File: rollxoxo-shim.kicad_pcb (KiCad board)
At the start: 4 copper layers, 70 parts, among them J1 USB_C_Receptacle_USB2.0_14P, J2 Conn_01x02, J3 Conn_01x10, J4 Conn_01x01, J5 Conn_01x10, J6 Conn_01x03, J7 Conn_01x01, SW1 SW_Push, SW2 SW_Push, U1 SN74LV1T125DBV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

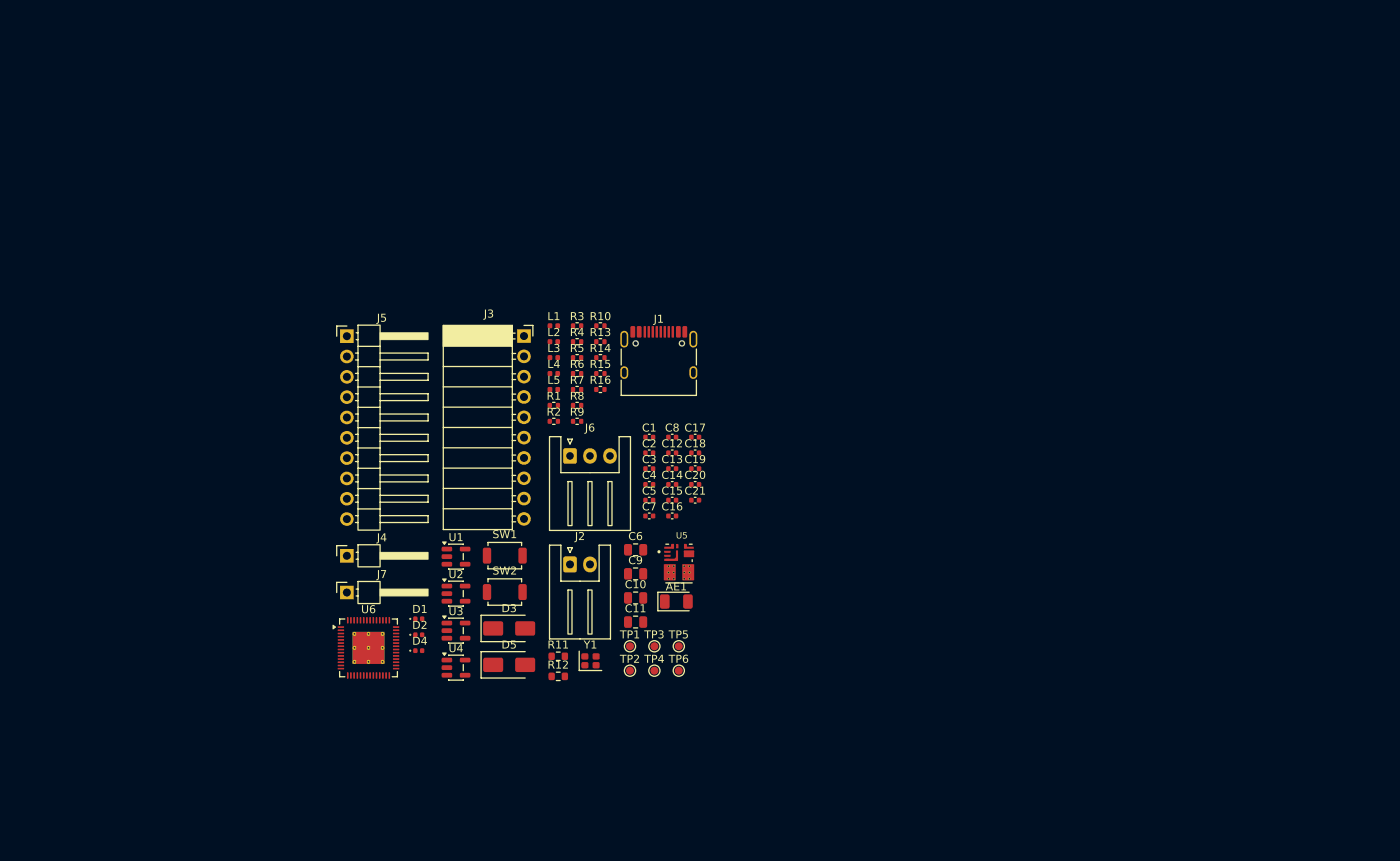
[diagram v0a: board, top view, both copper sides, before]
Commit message: pcb: initial rough placement
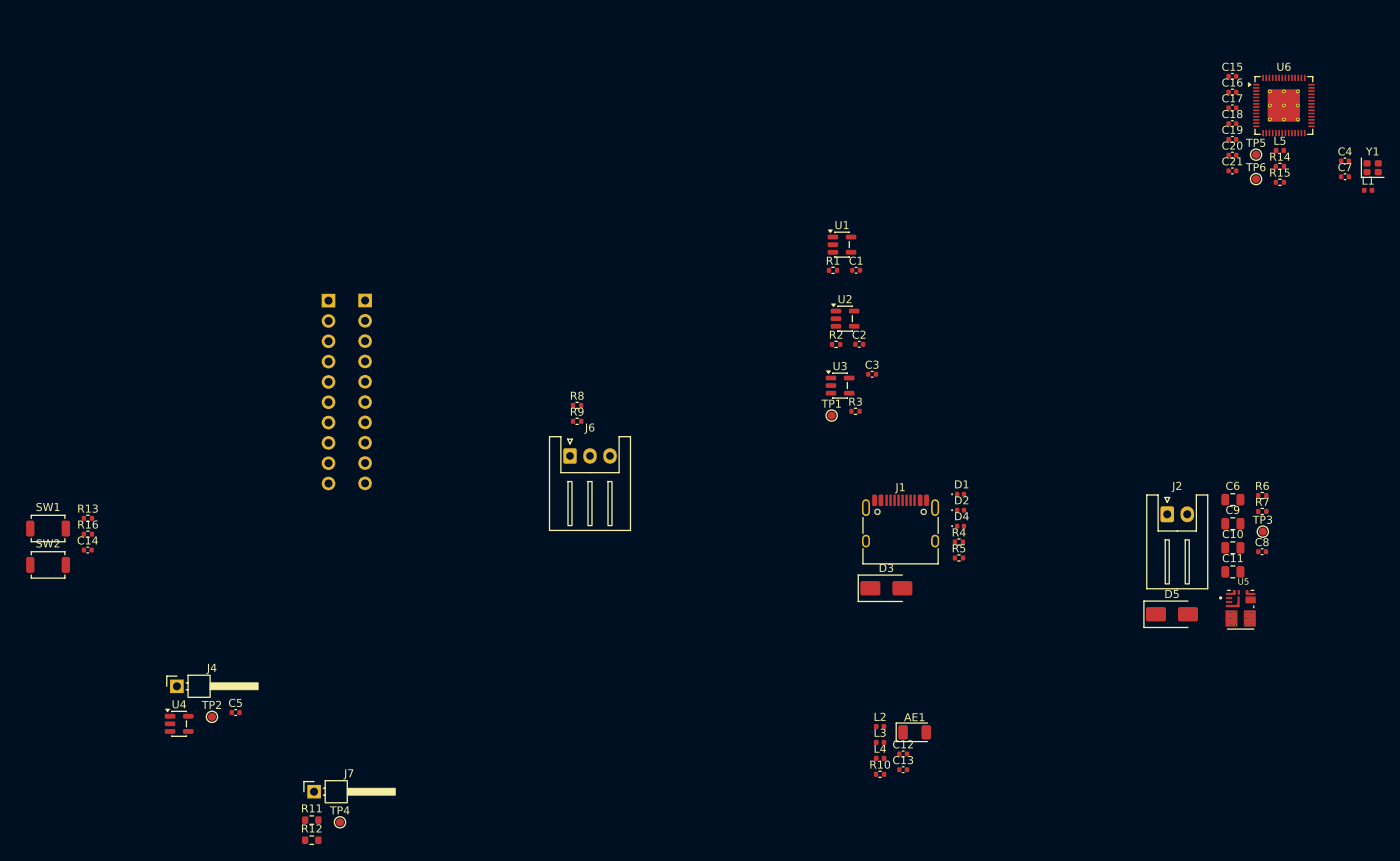
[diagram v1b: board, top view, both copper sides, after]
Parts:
- J3, J5: moved to B.Cu
- moved U6 133.0 mm to (187.0, 96.4)
- moved Y1 115.6 mm to (198.1, 104.2)
- moved L1 103.2 mm to (197.5, 107.0)
- moved C7 96.8 mm to (194.6, 105.3)
- moved C4 95.9 mm to (194.6, 103.3)
- moved L5 95.6 mm to (186.5, 102.0)
- moved TP6 94.8 mm to (183.5, 105.6)
- moved TP5 94.8 mm to (183.5, 102.5)
- moved R14 88.2 mm to (186.5, 104.0)
- moved R15 88.2 mm to (186.5, 106.0)
- moved C15 87.8 mm to (180.6, 92.8)
- moved C16 87.8 mm to (180.6, 94.7)
- moved R6 87.0 mm to (184.3, 145.2)
- moved R7 87.0 mm to (184.3, 147.2)
- moved D5 83.1 mm to (173.0, 160.0)
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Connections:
- J3 pad 1: /DOWN_BTN -> /UP_BTN
- J3 pad 10: /UP_BTN -> /DOWN_BTN
- J3 pad 4: +5V -> Net-(J3-Pin_4)
- J3 pad 5: /STOP_BTN -> Net-(J3-Pin_5)
- J3 pad 6: Net-(J3-Pin_6) -> /STOP_BTN
- J3 pad 7: Net-(J3-Pin_7) -> +5V
- J5 pad 1: /DOWN_BTN -> /UP_BTN
- J5 pad 10: /UP_BTN -> /DOWN_BTN
- J5 pad 4: +5V -> Net-(J3-Pin_4)
- J5 pad 5: /STOP_BTN -> Net-(J3-Pin_5)
- J5 pad 6: Net-(J3-Pin_6) -> /STOP_BTN
- J5 pad 7: Net-(J3-Pin_7) -> +5V

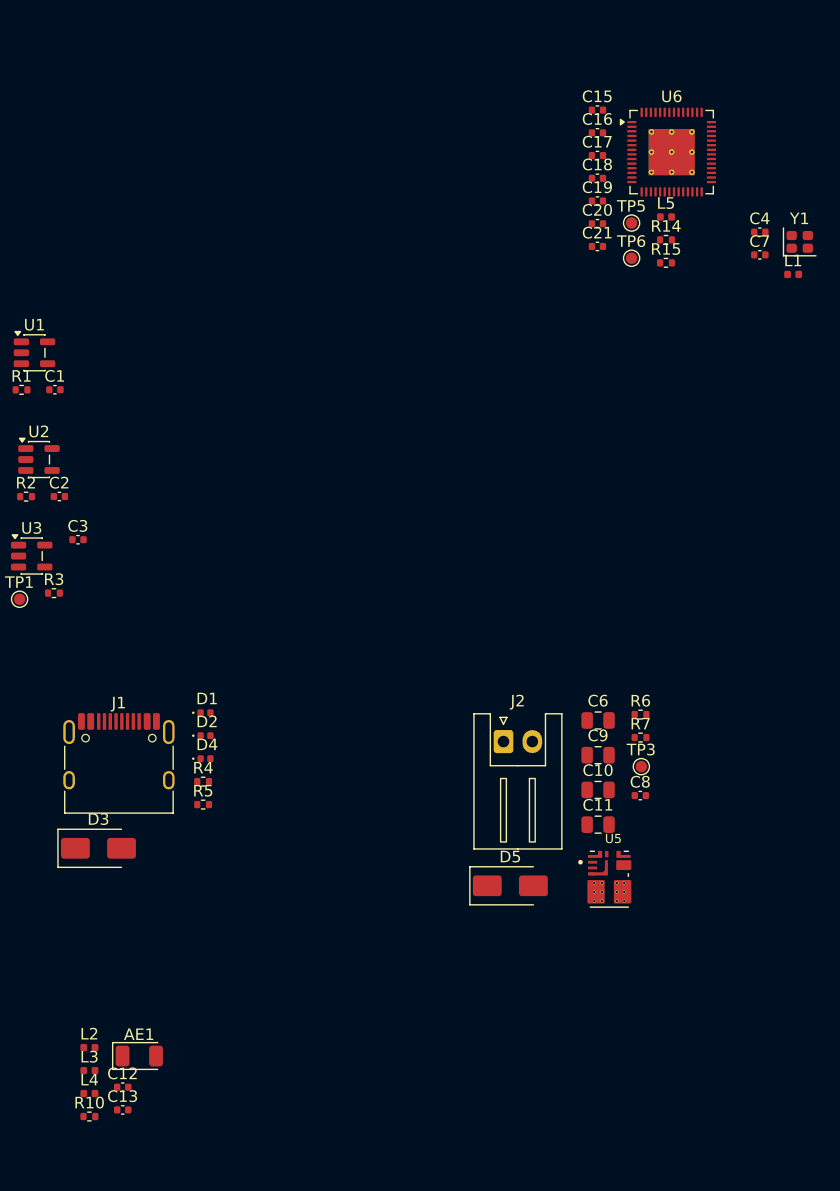
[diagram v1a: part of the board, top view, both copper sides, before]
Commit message: pcb: add esp32 layout
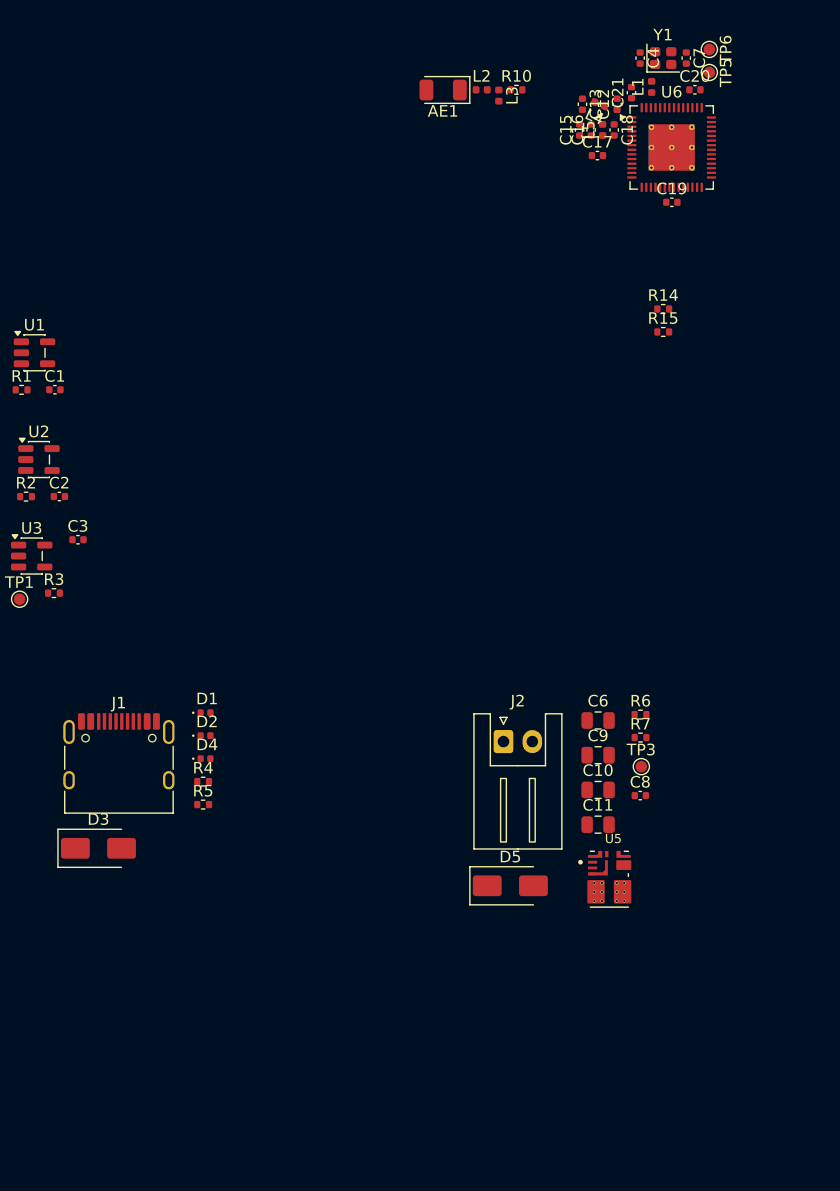
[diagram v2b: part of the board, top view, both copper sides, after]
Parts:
- moved L4 96.5 mm to (180.8, 92.2), turned to 157.5 degrees
- moved R10 96.4 mm to (173.5, 91.0)
- moved C13 95.9 mm to (179.2, 92.2), turned to -90 degrees
- moved C12 95.4 mm to (182.2, 92.2), turned to 90 degrees
- moved L3 91.7 mm to (172.0, 91.5), turned to -90 degrees
- moved L2 89.7 mm to (170.5, 91.0)
- moved AE1 87.8 mm to (167.2, 91.0), turned to 180 degrees
- moved L1 20.4 mm to (185.2, 90.8), turned to 90 degrees
- moved Y1 19.8 mm to (186.2, 88.2)
- moved TP6 19.3 mm to (190.2, 87.5), turned to -90 degrees
- moved C4 18.3 mm to (184.2, 88.2), turned to -90 degrees
- moved C7 18.2 mm to (188.2, 88.2), turned to -90 degrees
- moved TP5 14.7 mm to (190.2, 89.5), turned to -90 degrees
- moved C20 14.4 mm to (189.0, 91.0)
- moved C21 13.7 mm to (183.5, 91.2), turned to 90 degrees
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
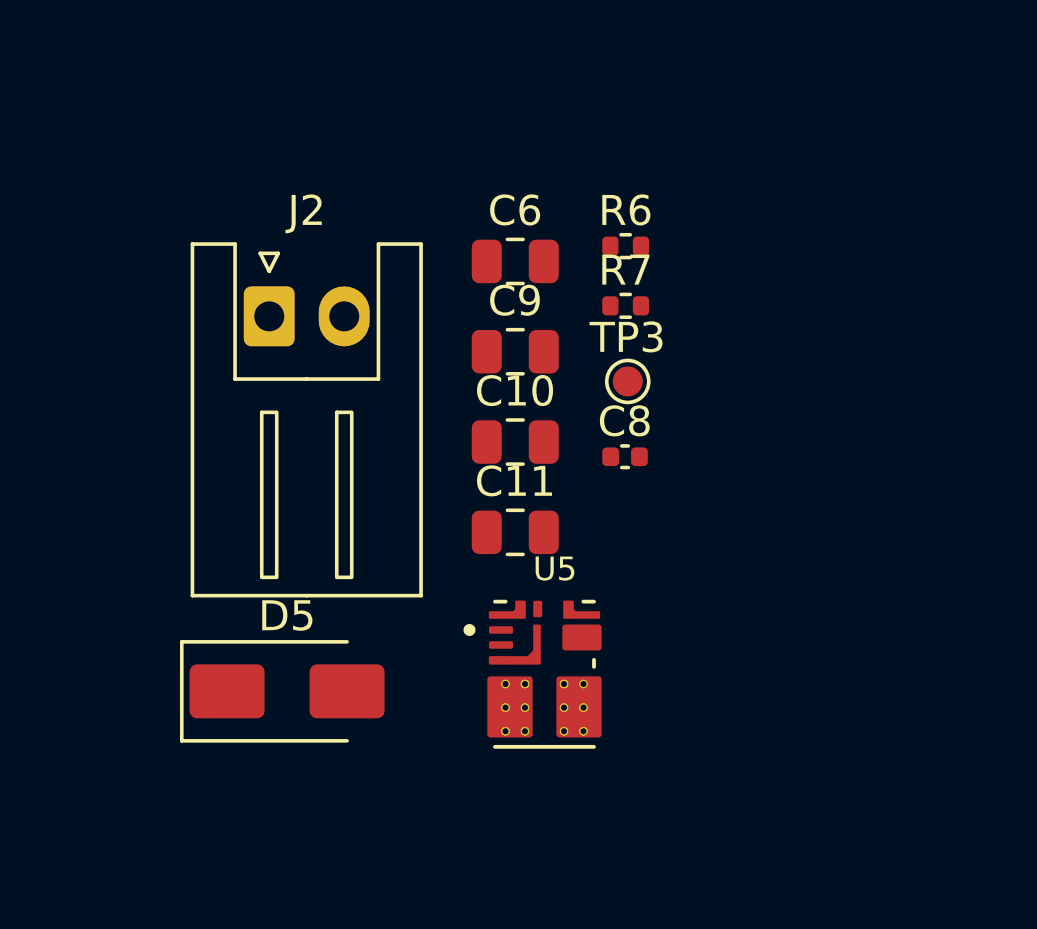
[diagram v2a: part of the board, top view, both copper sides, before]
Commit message: pcb: add +3v3 pwr module layout
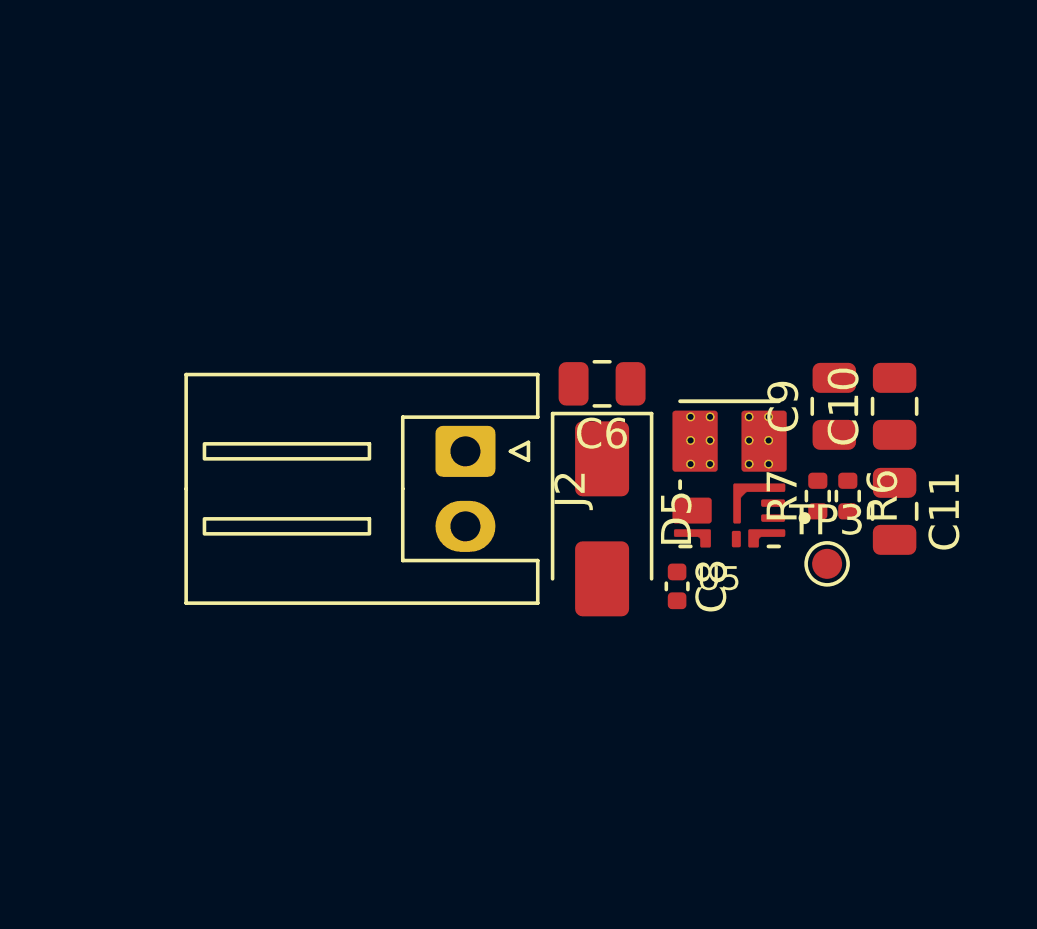
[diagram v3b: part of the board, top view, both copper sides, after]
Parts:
- moved C10 12.7 mm to (193.2, 150.5), turned to 90 degrees
- moved C11 12.7 mm to (193.2, 154.0), turned to -90 degrees
- moved D5 12.0 mm to (183.5, 154.2), turned to -90 degrees
- moved R6 11.1 mm to (191.7, 153.5), turned to -90 degrees
- moved C9 10.8 mm to (191.2, 150.5), turned to 90 degrees
- moved U5 9.09 mm to (187.8, 152.8), turned to 180 degrees
- moved R7 9.01 mm to (190.7, 153.5), turned to 90 degrees
- moved TP3 9.01 mm to (191.0, 155.8)
- moved J2 7.94 mm to (178.9, 152.0), turned to -90 degrees
- moved C6 5.00 mm to (183.5, 149.8), turned to 180 degrees
- moved C8 4.66 mm to (186.0, 156.5), turned to -90 degrees

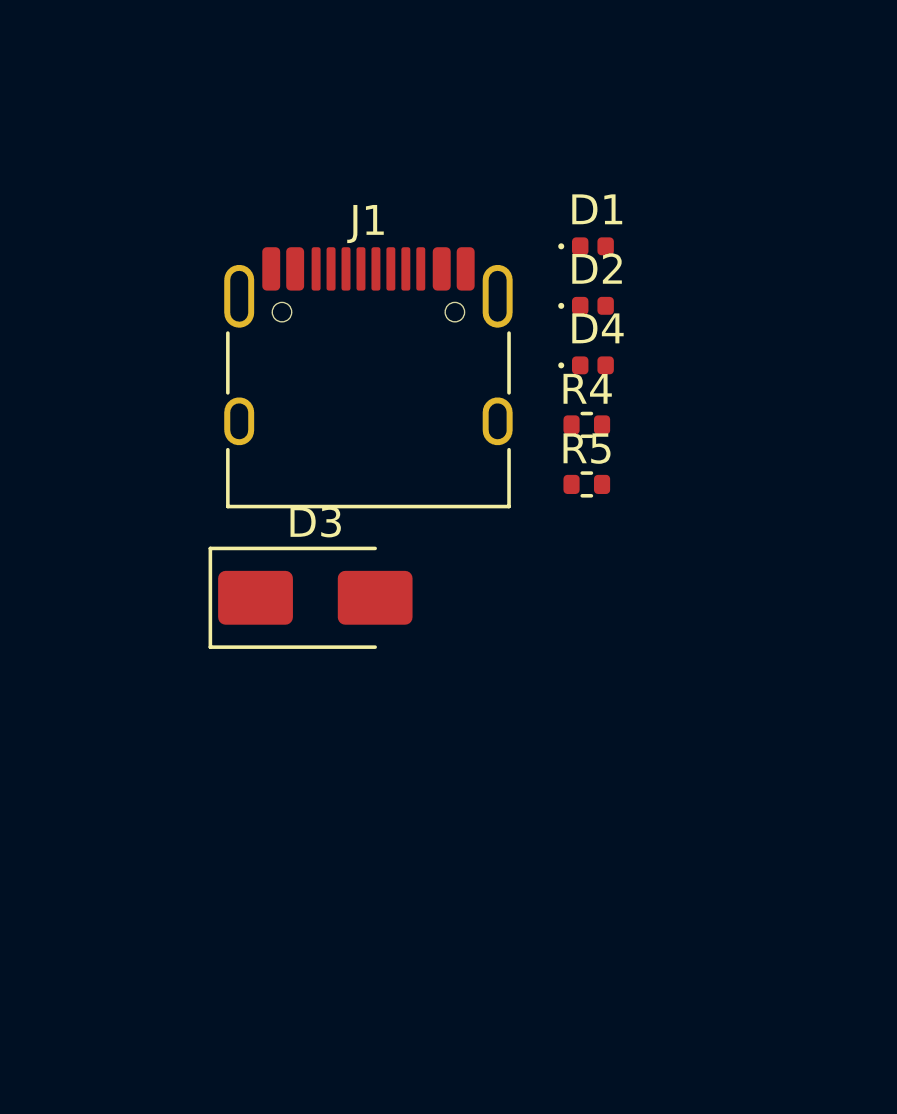
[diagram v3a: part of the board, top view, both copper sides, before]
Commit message: pcb: add usb layout
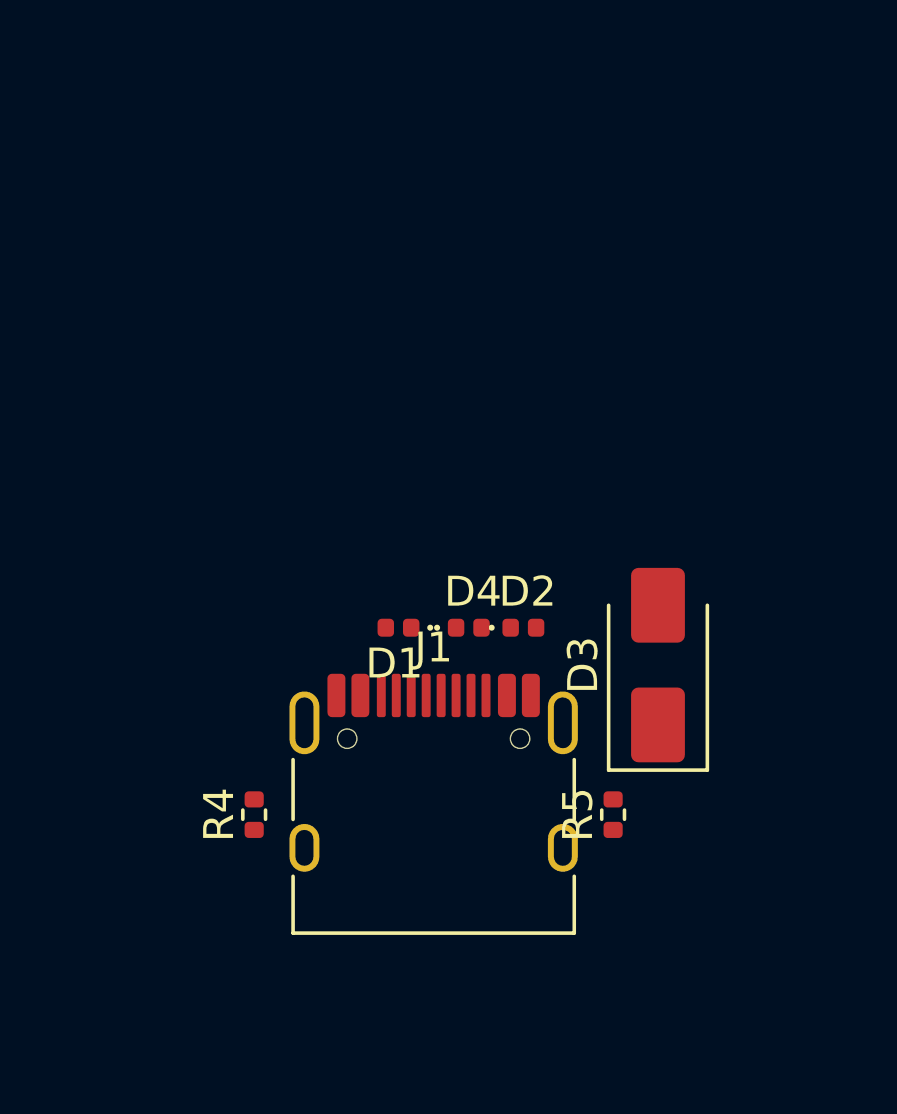
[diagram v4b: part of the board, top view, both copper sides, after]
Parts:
- moved R4 17.1 mm to (135.2, 164.0), turned to 90 degrees
- moved J1 14.4 mm to (141.2, 164.1)
- moved D1 14.3 mm to (140.1, 157.8), turned to 180 degrees
- moved D3 11.7 mm to (148.8, 159.0), turned to 90 degrees
- moved R5 11.1 mm to (147.2, 164.0), turned to 90 degrees
- moved D2 11.0 mm to (144.2, 157.8)
- moved D4 9.70 mm to (142.4, 157.8)

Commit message: pcb: add all layout
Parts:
- J4, J7, TP1: moved to B.Cu
- moved R12 18.2 mm to (69.8, 170.6), turned to -90 degrees
- moved R11 16.2 mm to (71.2, 170.6), turned to 90 degrees
- moved TP4 15.5 mm to (68.0, 170.6)
- moved J7 13.8 mm to (73.2, 170.6), turned to 180 degrees
- moved R13 10.2 mm to (31.5, 156.2)
- moved R3 7.54 mm to (131.0, 127.5)
- moved TP1 6.43 mm to (131.0, 128.8), turned to 180 degrees
- moved R16 6.36 mm to (31.2, 148.8), turned to 180 degrees
- moved C14 5.85 mm to (33.5, 156.2)
- moved C2 5.58 mm to (133.0, 120.8), turned to 180 degrees
- moved R2 5.52 mm to (131.0, 120.8)
- moved U4 5.15 mm to (51.0, 169.0)
- moved C5 4.61 mm to (54.2, 168.0)
- moved C3 3.55 mm to (133.0, 127.5), turned to 180 degrees
- moved TP2 3.32 mm to (54.2, 169.8)
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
